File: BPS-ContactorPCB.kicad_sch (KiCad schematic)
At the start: 3 parts, among them J1 Conn_01x04, J2 Conn_01x04, J3 Conn_01x02

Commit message: done
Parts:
- removed J3: Conn_01x02, UTSVT_Connectors:Molex_MicroFit3.0_1x2xP3.00mm_PolarizingPeg_Vertical, symbol Connector_Generic:Conn_01x02
- added J2: Conn_01x02, UTSVT_Connectors:Molex_MicroFit3.0_1x2xP3.00mm_PolarizingPeg_Vertical, symbol Connector_Generic:Conn_01x02
- added J4: Conn_01x04, UTSVT_Connectors:Molex_MicroFit3.0_1x4xP3.00mm_PolarizingPeg_Vertical, symbol Connector_Generic:Conn_01x04
- renumbered J2 to J3
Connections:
- net CONTACTOR_V+: now also J2.1 (Pin_1); no longer J3.1 (Pin_1)
- net CONTACTOR_V-: now also J4.2 (Pin_2)
- new net ESTOP: J2.2 (Pin_2), J3.1 (Pin_1), J4.1 (Pin_1)
- no-connect marks 0 -> 2
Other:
- moved on the sheet: J1
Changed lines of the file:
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@@
 	(generator_version "8.0")
 	(paper "A4")
-	(wire
-		(pts
-			(xy 38.1 63.5) (xy 59.69 63.5)
-		)
-		(stroke
-			(width 0)
-			(type default)
-		)
-	)
-	(wire
-		(pts
-			(xy 38.1 68.58) (xy 59.69 68.58)
+	(no_connect
+		(at 59.69 96.52)
+	)
+	(no_connect
+		(at 59.69 93.98)
+	)
+	(wire
+		(pts
+			(xy 38.1 52.07) (xy 59.69 52.07)
+		)
+		(stroke
+			(width 0)
+			(type default)
+		)
+	)
+	(wire
+		(pts
+			(xy 38.1 64.77) (xy 59.69 64.77)
+		)
+		(stroke
+			(width 0)
+			(type default)
+		)
+	)
+	(wire
+		(pts
+			(xy 38.1 57.15) (xy 59.69 57.15)
 		)
 		(stroke
@@
 	(wire
 		(pts
-			(xy 38.1 60.96) (xy 59.69 60.96)
+			(xy 38.1 49.53) (xy 59.69 49.53)
 		)
 		(stroke
@@
 	(wire
 		(pts
+			(xy 38.1 67.31) (xy 59.69 67.31)
+		)
+		(stroke
+			(width 0)
+			(type default)
+		)
+	)
+	(wire
+		(pts
 			(xy 38.1 74.93) (xy 59.69 74.93)
 		)
@@
 	(wire
 		(pts
-			(xy 38.1 66.04) (xy 59.69 66.04)
+			(xy 38.1 54.61) (xy 59.69 54.61)
 		)
 		(stroke
@@
 		)
 	)
-	(label "CONTACTOR_V+"
-		(at 38.1 88.9 0)
+	(label "ESTOP"
+		(at 38.1 74.93 0)
 		(fields_autoplaced yes)
 		(effects
@@
 		)
 	)
+	(label "ESTOP"
+		(at 38.1 88.9 0)
+		(fields_autoplaced yes)
+		(effects
+			(font
+				(size 1.27 1.27)
+			)
+			(justify left bottom)
+		)
+	)
 	(label "AUX_1"
 		(at 38.1 80.01 0)
@@
 	)
 	(label "AUX_1"
-		(at 38.1 66.04 0)
+		(at 38.1 54.61 0)
 		(fields_autoplaced yes)
 		(effects
@@
 	)
 	(label "CONTACTOR_V+"
-		(at 38.1 60.96 0)
+		(at 38.1 49.53 0)
 		(fields_autoplaced yes)
 		(effects
@@
 		)
 	)
+	(label "CONTACTOR_V+"
+		(at 38.1 64.77 0)
+		(fields_autoplaced yes)
+		(effects
+			(font
+				(size 1.27 1.27)
+			)
+			(justify left bottom)
+		)
+	)
 	(label "AUX_2"
-		(at 38.1 68.58 0)
-		(fields_autoplaced yes)
-		(effects
-			(font
-				(size 1.27 1.27)
-			)
-			(justify left bottom)
-		)
-	)
-	(label "CONTACTOR_V+"
-		(at 38.1 74.93 0)
+		(at 38.1 57.15 0)
+		(fields_autoplaced yes)
+		(effects
+			(font
+				(size 1.27 1.27)
+			)
+			(justify left bottom)
+		)
+	)
+	(label "ESTOP"
+		(at 38.1 67.31 0)
 		(fields_autoplaced yes)
 		(effects
@@
 	)
 	(label "CONTACTOR_V-"
-		(at 38.1 63.5 0)
+		(at 38.1 52.07 0)
 		(fields_autoplaced yes)
 		(effects
@@
 	)
 	(symbol
-		(lib_id "Connector_Generic:Conn_01x04")
-		(at 64.77 63.5 0)
+		(lib_id "Connector_Generic:Conn_01x02")
+		(at 64.77 64.77 0)
 		(unit 1)
 		(exclude_from_sim no)
@@
 		(dnp no)
 		(fields_autoplaced yes)
-		(property "Reference" "J1"
-			(at 67.31 63.4999 0)
-			(effects
-				(font
-					(size 1.27 1.27)
-				)
-				(justify left)
-			)
-		)
-		(property "Value" "Conn_01x04"
-			(at 67.31 66.0399 0)
-			(effects
-				(font
-					(size 1.27 1.27)
-				)
-				(justify left)
-			)
-		)
-		(property "Footprint" "UTSVT_Connectors:Molex_MicroFit3.0_1x4xP3.00mm_PolarizingPeg_Vertical"
-			(at 64.77 63.5 0)
+		(property "Reference" "J2"
+			(at 67.31 64.7699 0)
+			(effects
+				(font
+					(size 1.27 1.27)
+				)
+				(justify left)
+			)
+		)
+		(property "Value" "Conn_01x02"
+			(at 67.31 67.3099 0)
+			(effects
+				(font
+					(size 1.27 1.27)
+				)
+				(justify left)
+			)
+		)
+		(property "Footprint" "UTSVT_Connectors:Molex_MicroFit3.0_1x2xP3.00mm_PolarizingPeg_Vertical"
+			(at 64.77 64.77 0)
 			(effects
 				(font
@@
 		)
 		(property "Datasheet" "~"
-			(at 64.77 63.5 0)
-			(effects
-				(font
-					(size 1.27 1.27)
-				)
-				(hide yes)
-			)
-		)
-		(property "Description" "Generic connector, single row, 01x04, script generated (kicad-library-utils/schlib/autogen/connector/)"
-			(at 64.77 63.5 0)
+			(at 64.77 64.77 0)
+			(effects
+				(font
+					(size 1.27 1.27)
+				)
+				(hide yes)
+			)
+		)
+		(property "Description" "Generic connector, single row, 01x02, script generated (kicad-library-utils/schlib/autogen/connector/)"
+			(at 64.77 64.77 0)
 			(effects
 				(font
@@
 		(pin "2"
 		)
-		(pin "4"
-		)
 		(pin "1"
 		)
-		(pin "3"
-		)
 		(instances
-			(project "BPS-ContactorSplitterPCB"
+			(project "BPS-ContactorPCB"
 				(path "/dfb69ff1-8ca1-40c4-96ce-fa4f0ad1558b"
-					(reference "J1")
+					(reference "J2")
 					(unit 1)
 				)
@@
 	)
 	(symbol
-		(lib_id "Connector_Generic:Conn_01x02")
-		(at 64.77 88.9 0)
+		(lib_id "Connector_Generic:Conn_01x04")
+		(at 64.77 52.07 0)
 		(unit 1)
 		(exclude_from_sim no)
@@
 		(dnp no)
 		(fields_autoplaced yes)
-		(property "Reference" "J3"
-			(at 67.31 88.8999 0)
-			(effects
-				(font
-					(size 1.27 1.27)
-				)
-				(justify left)
-			)
-		)
-		(property "Value" "Conn_01x02"
-			(at 67.31 91.4399 0)
-			(effects
-				(font
-					(size 1.27 1.27)
-				)
-				(justify left)
-			)
-		)
-		(property "Footprint" "UTSVT_Connectors:Molex_MicroFit3.0_1x2xP3.00mm_PolarizingPeg_Vertical"
-			(at 64.77 88.9 0)
+		(property "Reference" "J1"
+			(at 67.31 52.0699 0)
+			(effects
+				(font
+					(size 1.27 1.27)
+				)
+				(justify left)
+			)
+		)
+		(property "Value" "Conn_01x04"
+			(at 67.31 54.6099 0)
+			(effects
+				(font
+					(size 1.27 1.27)
+				)
+				(justify left)
+			)
+		)
+		(property "Footprint" "UTSVT_Connectors:Molex_MicroFit3.0_1x4xP3.00mm_PolarizingPeg_Vertical"
+			(at 64.77 52.07 0)
 			(effects
 				(font
@@
 		)
 		(property "Datasheet" "~"
-			(at 64.77 88.9 0)
-			(effects
-				(font
-					(size 1.27 1.27)
-				)
-				(hide yes)
-			)
-		)
-		(property "Description" "Generic connector, single row, 01x02, script generated (kicad-library-utils/schlib/autogen/connector/)"
-			(at 64.77 88.9 0)
+			(at 64.77 52.07 0)
+			(effects
+				(font
+					(size 1.27 1.27)
+				)
+				(hide yes)
+			)
+		)
+		(property "Description" "Generic connector, single row, 01x04, script generated (kicad-library-utils/schlib/autogen/connector/)"
+			(at 64.77 52.07 0)
 			(effects
 				(font
@@
 		(pin "2"
 		)
+		(pin "4"
+		)
 		(pin "1"
 		)
+		(pin "3"
+		)
 		(instances
-			(project "BPS-ContactorSplitterPCB"
+			(project "BPS-ContactorPCB"
 				(path "/dfb69ff1-8ca1-40c4-96ce-fa4f0ad1558b"
-					(reference "J3")
+					(reference "J1")
 					(unit 1)
 				)
@@
 		(dnp no)
 		(fields_autoplaced yes)
-		(property "Reference" "J2"
+		(property "Reference" "J3"
 			(at 67.31 77.4699 0)
 			(effects
@@
 		)
 		(instances
-			(project "BPS-ContactorSplitterPCB"
+			(project "BPS-ContactorPCB"
 				(path "/dfb69ff1-8ca1-40c4-96ce-fa4f0ad1558b"
-					(reference "J2")
+					(reference "J3")
 					(unit 1)
 				)
+			)
+		)
+	)
+	(symbol
+		(lib_id "Connector_Generic:Conn_01x04")
+		(at 64.77 91.44 0)
+		(unit 1)
+		(exclude_from_sim no)
+		(in_bom yes)
+		(on_board yes)
+		(dnp no)
+		(fields_autoplaced yes)
+		(property "Reference" "J4"
+			(at 67.31 91.4399 0)
+			(effects
+				(font
+					(size 1.27 1.27)
+				)
+				(justify left)
+			)
+		)
+		(property "Value" "Conn_01x04"
+			(at 67.31 93.9799 0)
+			(effects
+				(font
+					(size 1.27 1.27)
+				)
+				(justify left)
+			)
+		)
+		(property "Footprint" "UTSVT_Connectors:Molex_MicroFit3.0_1x4xP3.00mm_PolarizingPeg_Vertical"
+			(at 64.77 91.44 0)
+			(effects
+				(font
+					(size 1.27 1.27)
+				)
+				(hide yes)
+			)
+		)
+		(property "Datasheet" "~"
+			(at 64.77 91.44 0)
+			(effects
+				(font
+					(size 1.27 1.27)
+				)
+				(hide yes)
+			)
+		)
+		(property "Description" "Generic connector, single row, 01x04, script generated (kicad-library-utils/schlib/autogen/connector/)"
+			(at 64.77 91.44 0)
+			(effects
+				(font
+					(size 1.27 1.27)
+				)
+				(hide yes)
+			)
+		)
+		(pin "2"
+		)
+		(pin "4"
+		)
+		(pin "1"
+		)
+		(pin "3"
+		)
+		(instances
+			(project "BPS-ContactorPCB"
+				(path "/dfb69ff1-8ca1-40c4-96ce-fa4f0ad1558b"
+					(reference "J4")
+					(unit 1)
+				)

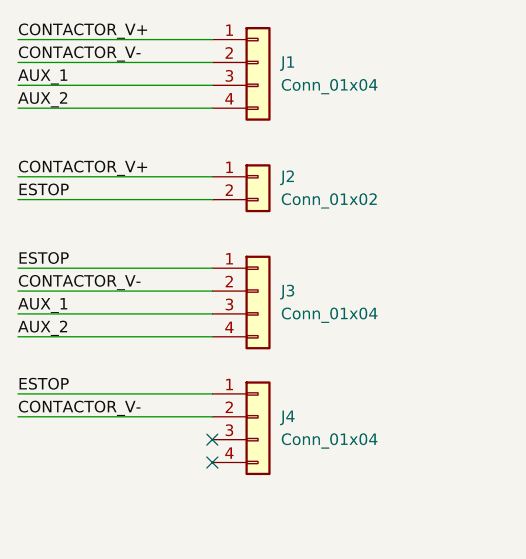
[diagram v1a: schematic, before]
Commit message: Added 2nd ESTOP
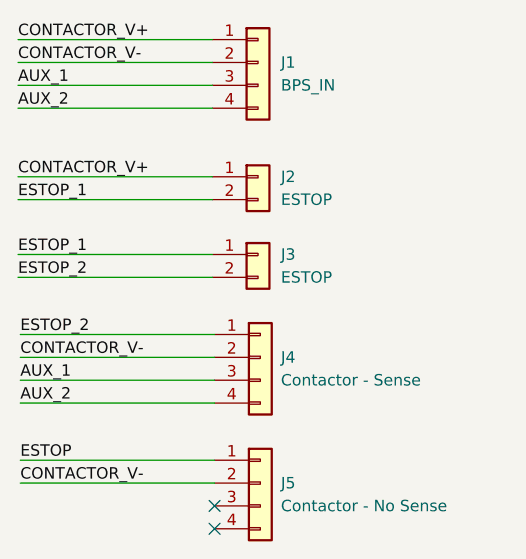
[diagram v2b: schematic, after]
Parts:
- added J3: ESTOP, UTSVT_Connectors:Molex_MicroFit3.0_1x2xP3.00mm_PolarizingPeg_Vertical, symbol Connector_Generic:Conn_01x02
- J1: value Conn_01x04 -> BPS_IN
- J2: value Conn_01x02 -> ESTOP
- J4: renamed from J3; value Conn_01x04 -> Contactor - Sense
- J5: renamed from J4; value Conn_01x04 -> Contactor - No Sense
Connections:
- net ESTOP: no longer J2.2 (Pin_2), J4.1 (Pin_1)
- new net ESTOP_1: J2.2 (Pin_2), J3.1 (Pin_1)
- new net ESTOP_2: J3.2 (Pin_2), J4.1 (Pin_1)
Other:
- moved on the sheet: J4, J5
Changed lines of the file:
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@@
 	(paper "A4")
 	(no_connect
-		(at 59.69 96.52)
+		(at 59.944 103.886)
 	)
 	(no_connect
-		(at 59.69 93.98)
+		(at 59.944 101.346)
 	)
 	(wire
@@
 	(wire
 		(pts
-			(xy 38.1 80.01) (xy 59.69 80.01)
-		)
-		(stroke
-			(width 0)
-			(type default)
-		)
-	)
-	(wire
-		(pts
-			(xy 38.1 88.9) (xy 59.69 88.9)
+			(xy 38.1 75.946) (xy 59.69 75.946)
+		)
+		(stroke
+			(width 0)
+			(type default)
+		)
+	)
+	(wire
+		(pts
+			(xy 38.354 87.376) (xy 59.944 87.376)
+		)
+		(stroke
+			(width 0)
+			(type default)
+		)
+	)
+	(wire
+		(pts
+			(xy 38.354 96.266) (xy 59.944 96.266)
+		)
+		(stroke
+			(width 0)
+			(type default)
+		)
+	)
+	(wire
+		(pts
+			(xy 38.1 73.406) (xy 59.69 73.406)
 		)
 		(stroke
@@
 	(wire
 		(pts
-			(xy 38.1 82.55) (xy 59.69 82.55)
+			(xy 38.354 89.916) (xy 59.944 89.916)
 		)
 		(stroke
@@
 	(wire
 		(pts
-			(xy 38.1 74.93) (xy 59.69 74.93)
-		)
-		(stroke
-			(width 0)
-			(type default)
-		)
-	)
-	(wire
-		(pts
-			(xy 38.1 77.47) (xy 59.69 77.47)
+			(xy 38.354 82.296) (xy 59.944 82.296)
+		)
+		(stroke
+			(width 0)
+			(type default)
+		)
+	)
+	(wire
+		(pts
+			(xy 38.354 84.836) (xy 59.944 84.836)
 		)
 		(stroke
@@
 	(wire
 		(pts
-			(xy 38.1 91.44) (xy 59.69 91.44)
-		)
-		(stroke
-			(width 0)
-			(type default)
+			(xy 38.354 98.806) (xy 59.944 98.806)
+		)
+		(stroke
+			(width 0)
+			(type default)
+		)
+	)
+	(label "ESTOP_2"
+		(at 38.354 82.296 0)
+		(fields_autoplaced yes)
+		(effects
+			(font
+				(size 1.27 1.27)
+			)
+			(justify left bottom)
+		)
+	)
+	(label "AUX_2"
+		(at 38.354 89.916 0)
+		(fields_autoplaced yes)
+		(effects
+			(font
+				(size 1.27 1.27)
+			)
+			(justify left bottom)
+		)
+	)
+	(label "CONTACTOR_V-"
+		(at 38.354 98.806 0)
+		(fields_autoplaced yes)
+		(effects
+			(font
+				(size 1.27 1.27)
+			)
+			(justify left bottom)
 		)
 	)
 	(label "ESTOP"
-		(at 38.1 74.93 0)
-		(fields_autoplaced yes)
-		(effects
-			(font
-				(size 1.27 1.27)
-			)
-			(justify left bottom)
-		)
-	)
-	(label "AUX_2"
-		(at 38.1 82.55 0)
-		(fields_autoplaced yes)
-		(effects
-			(font
-				(size 1.27 1.27)
-			)
-			(justify left bottom)
-		)
-	)
-	(label "CONTACTOR_V-"
-		(at 38.1 91.44 0)
-		(fields_autoplaced yes)
-		(effects
-			(font
-				(size 1.27 1.27)
-			)
-			(justify left bottom)
-		)
-	)
-	(label "ESTOP"
-		(at 38.1 88.9 0)
+		(at 38.354 96.266 0)
 		(fields_autoplaced yes)
 		(effects
@@
 	)
 	(label "AUX_1"
-		(at 38.1 80.01 0)
+		(at 38.354 87.376 0)
 		(fields_autoplaced yes)
 		(effects
@@
 		)
 	)
+	(label "ESTOP_2"
+		(at 38.1 75.946 0)
+		(fields_autoplaced yes)
+		(effects
+			(font
+				(size 1.27 1.27)
+			)
+			(justify left bottom)
+		)
+	)
 	(label "CONTACTOR_V+"
 		(at 38.1 49.53 0)
@@
 	)
 	(label "CONTACTOR_V-"
-		(at 38.1 77.47 0)
+		(at 38.354 84.836 0)
 		(fields_autoplaced yes)
 		(effects
@@
 		)
 	)
-	(label "ESTOP"
+	(label "ESTOP_1"
+		(at 38.1 73.406 0)
+		(fields_autoplaced yes)
+		(effects
+			(font
+				(size 1.27 1.27)
+			)
+			(justify left bottom)
+		)
+	)
+	(label "ESTOP_1"
 		(at 38.1 67.31 0)
 		(fields_autoplaced yes)
@@
 			)
 			(justify left bottom)
+		)
+	)
+	(symbol
+		(lib_id "Connector_Generic:Conn_01x02")
+		(at 64.77 73.406 0)
+		(unit 1)
+		(exclude_from_sim no)
+		(in_bom yes)
+		(on_board yes)
+		(dnp no)
+		(fields_autoplaced yes)
+		(property "Reference" "J3"
+			(at 67.31 73.4059 0)
+			(effects
+				(font
+					(size 1.27 1.27)
+				)
+				(justify left)
+			)
+		)
+		(property "Value" "ESTOP"
+			(at 67.31 75.9459 0)
+			(effects
+				(font
+					(size 1.27 1.27)
+				)
+				(justify left)
+			)
+		)
+		(property "Footprint" "UTSVT_Connectors:Molex_MicroFit3.0_1x2xP3.00mm_PolarizingPeg_Vertical"
+			(at 64.77 73.406 0)
+			(effects
+				(font
+					(size 1.27 1.27)
+				)
+				(hide yes)
+			)
+		)
+		(property "Datasheet" "~"
+			(at 64.77 73.406 0)
+			(effects
+				(font
+					(size 1.27 1.27)
+				)
+				(hide yes)
+			)
+		)
+		(property "Description" "Generic connector, single row, 01x02, script generated (kicad-library-utils/schlib/autogen/connector/)"
+			(at 64.77 73.406 0)
+			(effects
+				(font
+					(size 1.27 1.27)
+				)
+				(hide yes)
+			)
+		)
+		(pin "2"
+		)
+		(pin "1"
+		)
+		(instances
+			(project "BPS-ContactorPCB"
+				(path "/dfb69ff1-8ca1-40c4-96ce-fa4f0ad1558b"
+					(reference "J3")
+					(unit 1)
+				)
+			)
 		)
 	)
@@
 			)
 		)
-		(property "Value" "Conn_01x02"
+		(property "Value" "ESTOP"
 			(at 67.31 67.3099 0)
 			(effects
@@
 			)
 		)
-		(property "Value" "Conn_01x04"
+		(property "Value" "BPS_IN"
 			(at 67.31 54.6099 0)
 			(effects
@@
 	(symbol
 		(lib_id "Connector_Generic:Conn_01x04")
-		(at 64.77 77.47 0)
+		(at 65.024 84.836 0)
 		(unit 1)
 		(exclude_from_sim no)
@@
 		(dnp no)
 		(fields_autoplaced yes)
-		(property "Reference" "J3"
-			(at 67.31 77.4699 0)
-			(effects
-				(font
-					(size 1.27 1.27)
-				)
-				(justify left)
-			)
-		)
-		(property "Value" "Conn_01x04"
-			(at 67.31 80.0099 0)
+		(property "Reference" "J4"
+			(at 67.31 84.8359 0)
+			(effects
+				(font
+					(size 1.27 1.27)
+				)
+				(justify left)
+			)
+		)
+		(property "Value" "Contactor - Sense"
+			(at 67.31 87.3759 0)
 			(effects
 				(font
@@
 		)
 		(property "Footprint" "UTSVT_Connectors:Molex_MicroFit3.0_1x4xP3.00mm_PolarizingPeg_Vertical"
-			(at 64.77 77.47 0)
+			(at 65.024 84.836 0)
 			(effects
 				(font
@@
 		)
 		(property "Datasheet" "~"
-			(at 64.77 77.47 0)
+			(at 65.024 84.836 0)
 			(effects
 				(font
@@
 		)
 		(property "Description" "Generic connector, single row, 01x04, script generated (kicad-library-utils/schlib/autogen/connector/)"
-			(at 64.77 77.47 0)
+			(at 65.024 84.836 0)
 			(effects
 				(font
@@
 			(project "BPS-ContactorPCB"
 				(path "/dfb69ff1-8ca1-40c4-96ce-fa4f0ad1558b"
-					(reference "J3")
+					(reference "J4")
 					(unit 1)
 				)
@@
 	(symbol
 		(lib_id "Connector_Generic:Conn_01x04")
-		(at 64.77 91.44 0)
+		(at 65.024 98.806 0)
 		(unit 1)
 		(exclude_from_sim no)
@@
 		(dnp no)
 		(fields_autoplaced yes)
-		(property "Reference" "J4"
-			(at 67.31 91.4399 0)
-			(effects
-				(font
-					(size 1.27 1.27)
-				)
-				(justify left)
-			)
-		)
-		(property "Value" "Conn_01x04"
-			(at 67.31 93.9799 0)
+		(property "Reference" "J5"
+			(at 67.31 98.8059 0)
+			(effects
+				(font
+					(size 1.27 1.27)
+				)
+				(justify left)
+			)
+		)
+		(property "Value" "Contactor - No Sense"
+			(at 67.31 101.3459 0)
 			(effects
 				(font
@@
 		)
 		(property "Footprint" "UTSVT_Connectors:Molex_MicroFit3.0_1x4xP3.00mm_PolarizingPeg_Vertical"
-			(at 64.77 91.44 0)
+			(at 65.024 98.806 0)
 			(effects
 				(font
@@
 		)
 		(property "Datasheet" "~"
-			(at 64.77 91.44 0)
+			(at 65.024 98.806 0)
 			(effects
 				(font
@@
 		)
 		(property "Description" "Generic connector, single row, 01x04, script generated (kicad-library-utils/schlib/autogen/connector/)"
-			(at 64.77 91.44 0)
+			(at 65.024 98.806 0)
 			(effects
 				(font
@@
 			(project "BPS-ContactorPCB"
 				(path "/dfb69ff1-8ca1-40c4-96ce-fa4f0ad1558b"
-					(reference "J4")
+					(reference "J5")
 					(unit 1)
 				)

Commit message: Add indicators
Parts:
- added D1: Driver E-Stop, LED_SMD:LED_0805_2012Metric, symbol Device:D
- added D2: External E-Stop, LED_SMD:LED_0805_2012Metric, symbol Device:D
- added D3: Contactor 1, LED_SMD:LED_0805_2012Metric, symbol Device:D
- added D4: Contactor 2, LED_SMD:LED_0805_2012Metric, symbol Device:D
- added J1: BPS_PWR, UTSVT_Connectors:Molex_MicroFit3.0_1x2xP3.00mm_PolarizingPeg_Vertical, symbol Connector_Generic:Conn_01x02
- added Q1, Q2: PMOS, symbol Simulation_SPICE:PMOS
- added R1: 510, symbol Device:R
- added R2, R4: 10k, Resistor_SMD:R_0805_2012Metric, symbol Device:R
- added R3, R5, R6, R7: 1.5k, Resistor_SMD:R_0805_2012Metric, symbol Device:R
- added U1: SFH617A-1, Package_DIP:DIP-4_W7.62mm, symbol Isolator:SFH617A-1
- J3: renamed from J2; value ESTOP -> DRV_ESTOP
- J4: renamed from J3; value ESTOP -> EXT_ESTOP
- J5: renamed from J4; value Contactor - Sense -> HV+ Contactor
- J6: renamed from J5; value Contactor - No Sense -> HV- Contactor
- renumbered J1 to J2
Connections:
- net ESTOP_2 is gone; now on net EXT_ESTOP: J4.2 (Pin_2), J5.1 (Pin_1)
- net +12V: now reaches J6.3 (Pin_3)
- net +12V: now also J5.3 (Pin_3), J1.1 (Pin_1), Q1.3 (S), Q2.3 (S)
- net C2_SENSE: now reaches J6.4 (Pin_4)
- net C2_SENSE: now also R7.1
- net AUX_1 renamed BPS_AUX_1
- net BPS_AUX_1: now also U1.4; no longer J5.3 (Pin_3)
- net AUX_2 renamed BPS_AUX_2
- net BPS_AUX_2: now also U1.3; no longer J5.4 (Pin_4)
- net ESTOP renamed EXT_ESTOP
- net EXT_ESTOP: now also Q2.2 (G), R4.1
- net ESTOP_1 renamed DRV_ESTOP
- net DRV_ESTOP: now also Q1.2 (G), R2.1
- new net: D2.2 (A), R5.2
- new net: R1.2, U1.1
- new net: Q1.1 (D), R3.1
- new net: D1.2 (A), R3.2
- new net: Q2.1 (D), R5.1
- new net: D4.2 (A), R7.2
- new net: D3.2 (A), R6.2
- new net C1_SENSE: J5.4 (Pin_4), R1.1, R6.1
- new net GNDPWR: D1.1 (K), D2.1 (K), D3.1 (K), D4.1 (K), J1.2 (Pin_2), R2.2, R4.2, U1.2
- no-connect marks 2 -> 0
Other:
- note added: "E-Stop LEDs - RED Contactor LEDs - GREEN"
- moved on the sheet: J2, J3, J4, J5, J6
